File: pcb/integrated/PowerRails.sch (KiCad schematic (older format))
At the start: 28 parts, among them U9001 EC6AW, U9002 RAC10, U9003 TPS82140, U9004 TPS82140, U9005 TPS735, U9006 TPS735

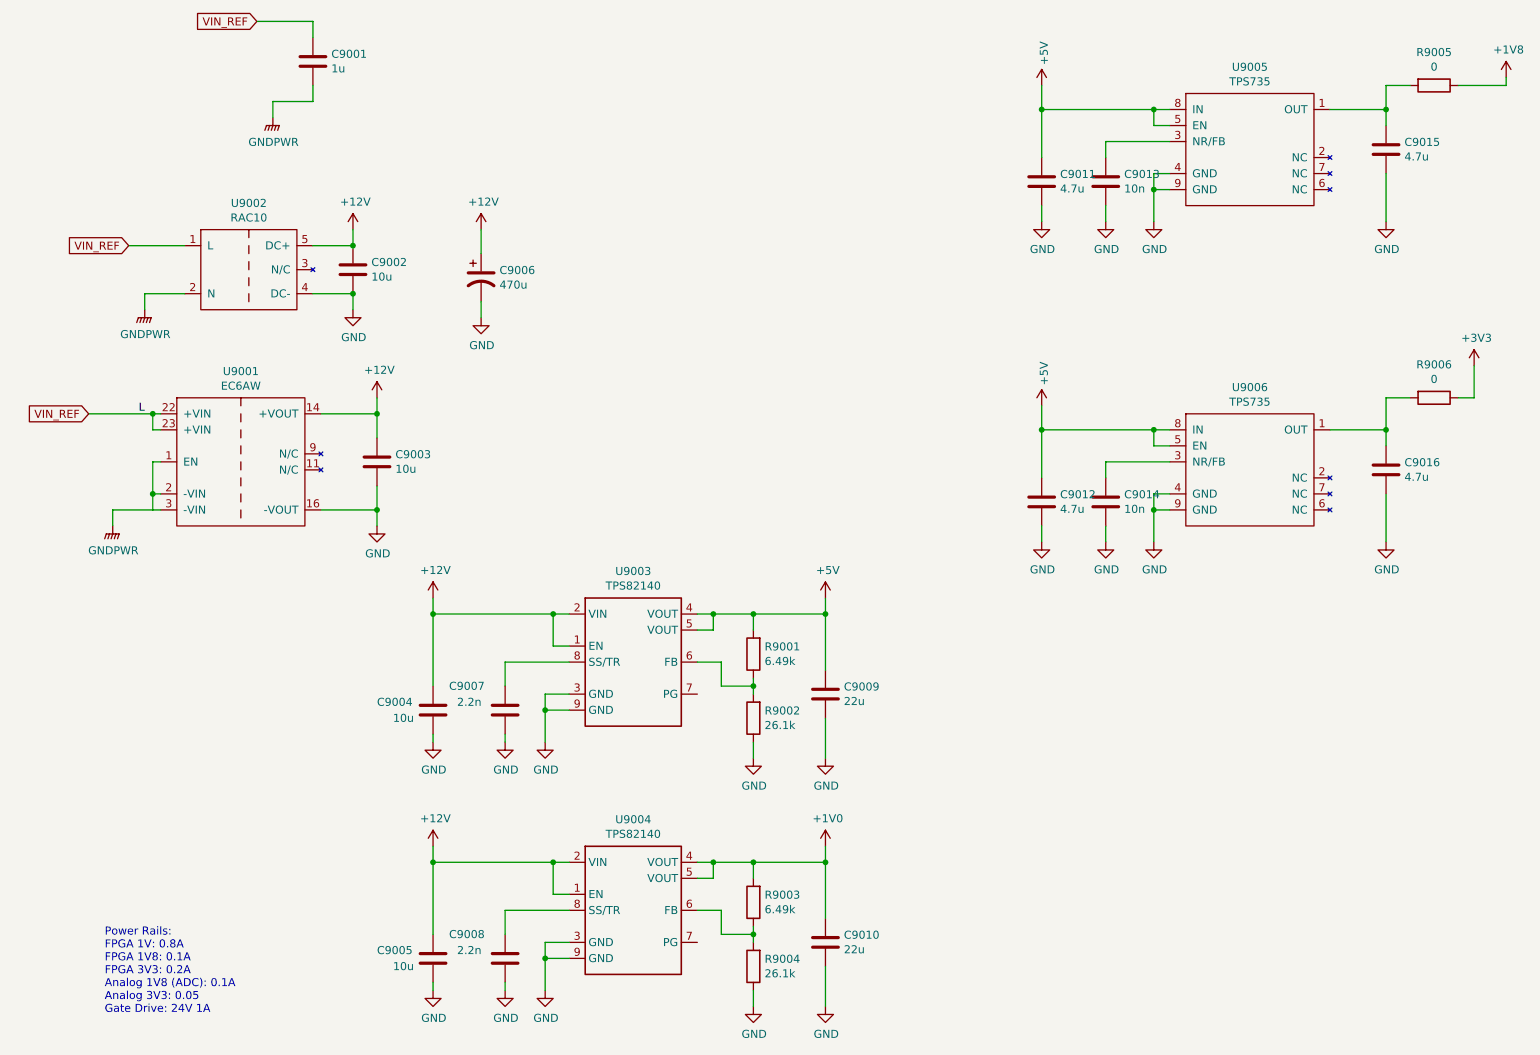
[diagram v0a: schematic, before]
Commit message: schematic fixes and component placement
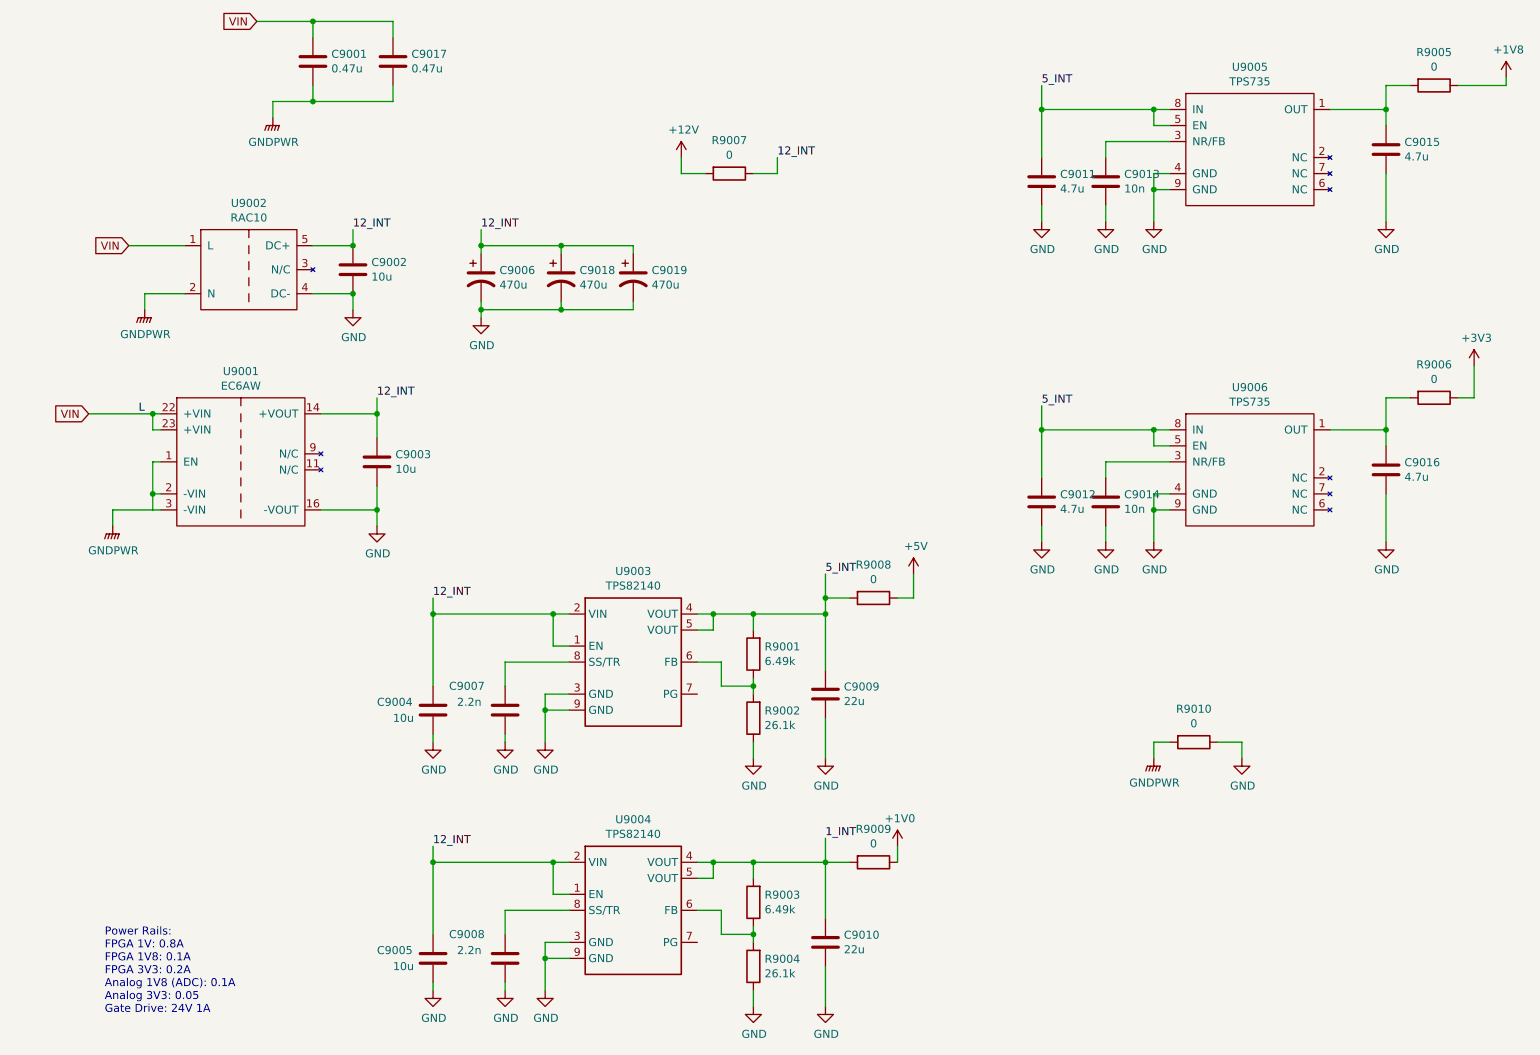
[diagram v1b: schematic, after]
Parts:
- added C9017: 0.47u, Capacitor_SMD:C_1812_4532Metric, symbol Device:C
- added C9018, C9019: 470u, Capacitor_THT:CP_Radial_D10.0mm_P5.00mm, symbol Device:CP1
- added R9007, R9008, R9009, R9010: 0, Resistor_SMD:R_0805_2012Metric, symbol Device:R
- C9001: value 1u -> 0.47u; footprint Capacitor_SMD:C_0805_2012Metric -> Capacitor_SMD:C_1812_4532Metric
- C9002, C9003, C9004, C9005: footprint Capacitor_SMD:C_0805_2012Metric -> Capacitor_SMD:C_1206_3216Metric
- C9007, C9008: footprint Capacitor_SMD:C_0805_2012Metric -> Capacitor_SMD:C_0402_1005Metric
- C9011, C9012, C9015, C9016: footprint Capacitor_SMD:C_0402_1005Metric -> Capacitor_SMD:C_0603_1608Metric
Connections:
- net +12V: now also R9007.2; no longer C9002.1, C9003.1, C9004.1, C9005.1, C9006.1, U9001.14 (+VOUT), U9002.5 (DC+), U9003.1 (EN), U9003.2 (VIN), U9004.1 (EN), U9004.2 (VIN)
- net +1V0: now also R9009.1; no longer C9010.1, R9003.2, U9004.4 (VOUT), U9004.5 (VOUT)
- net +5V: now also R9008.1; no longer C9009.1, C9011.2, C9012.2, R9001.2, U9003.4 (VOUT), U9003.5 (VOUT), U9005.5 (EN), U9005.8 (IN), U9006.5 (EN), U9006.8 (IN)
- net GND: now also C9018.2, C9019.2, R9010.1
- net GNDPWR: now also C9017.2, R9010.2
- net VIN_REF renamed VIN
- net VIN: now also C9017.1
- new net 12_INT: C9002.1, C9003.1, C9004.1, C9005.1, C9006.1, C9018.1, C9019.1, R9007.1, U9001.14 (+VOUT), U9002.5 (DC+), U9003.1 (EN), U9003.2 (VIN), U9004.1 (EN), U9004.2 (VIN)
- new net 1_INT: C9010.1, R9003.2, R9009.2, U9004.4 (VOUT), U9004.5 (VOUT)
- new net 5_INT: C9009.1, C9011.2, C9012.2, R9001.2, R9008.2, U9003.4 (VOUT), U9003.5 (VOUT), U9005.5 (EN), U9005.8 (IN), U9006.5 (EN), U9006.8 (IN)

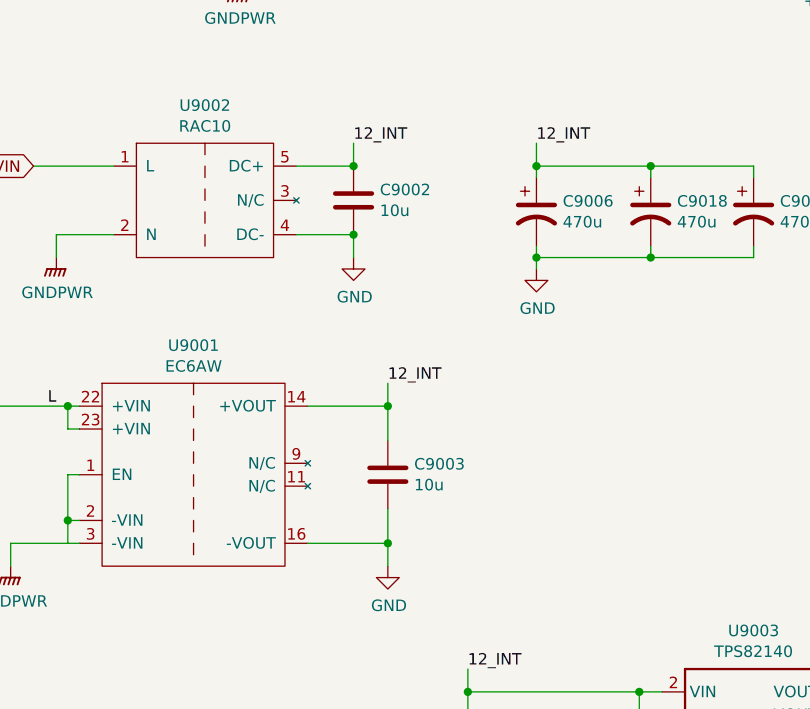
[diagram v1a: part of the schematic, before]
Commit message: routing, all componens placed on PCB
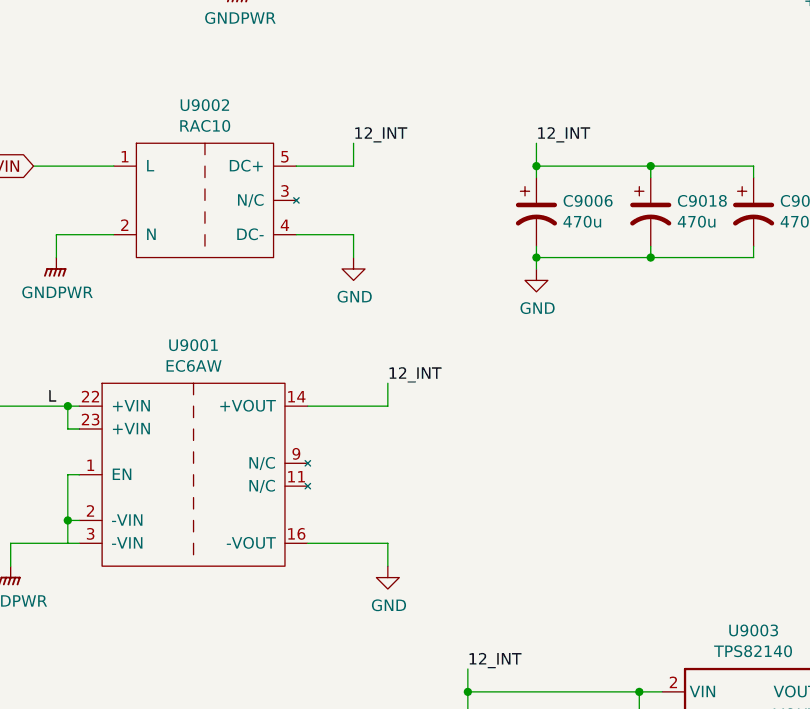
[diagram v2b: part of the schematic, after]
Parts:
- removed C9002, C9003: 10u, Capacitor_SMD:C_1206_3216Metric, symbol Device:C
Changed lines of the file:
@@
-	1    0    0    -1
-$EndComp
-$Comp
-L Device:C C9003
-U 1 1 5D6FA237
-P 3550 3750
-F 0 "C9003" H 3665 3796 50  0000 L CNN
-F 1 "10u" H 3665 3705 50  0000 L CNN
-F 2 "Capacitor_SMD:C_1206_3216Metric" H 3588 3600 50  0001 C CNN
-F 3 "~" H 3550 3750 50  0001 C CNN
-	1    3550 3750
-	1    0    0    -1
-$EndComp
-$Comp
-L Device:C C9002
-U 1 1 5D6FA2D9
-P 3400 2550
-F 0 "C9002" H 3515 2596 50  0000 L CNN
-F 1 "10u" H 3515 2505 50  0000 L CNN
-F 2 "Capacitor_SMD:C_1206_3216Metric" H 3438 2400 50  0001 C CNN
-F 3 "~" H 3400 2550 50  0001 C CNN
-	1    3400 2550
 	1    0    0    -1
 $EndComp
@@
 	3200 4050 3550 4050
 Wire Wire Line
-	3550 4050 3550 3900
-Wire Wire Line
 	3200 3450 3550 3450
 Wire Wire Line
-	3550 3450 3550 3600
-Wire Wire Line
 	3550 4050 3550 4150
-Connection ~ 3550 4050
 Wire Wire Line
 	3550 3450 3550 3350
-Connection ~ 3550 3450
 Wire Wire Line
 	3150 2700 3400 2700
@@
 Wire Wire Line
 	3400 2400 3400 2300
-Connection ~ 3400 2400
 Wire Wire Line
 	3400 2700 3400 2800
-Connection ~ 3400 2700
 $Comp
 L power:GND #PWR09003

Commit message: PCB routing finihsed, ready for design review
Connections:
- net VIN renamed VLINK
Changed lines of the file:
@@
 	1750 3450 2150 3450
 Text GLabel 2800 1000 0    50   Input ~ 0
-VIN
+VLINK
 $Comp
 L power:GNDPWR #PWR0103
@@
 	3650 1500 3650 1400
 Connection ~ 3150 1500
-Text GLabel 2000 2400 0    50   Input ~ 0
-VIN
-Text GLabel 1750 3450 0    50   Input ~ 0
-VIN
 $Comp
 L power:GND #PWR0177
@@
 Wire Wire Line
 	4700 2800 4200 2800
+Text GLabel 2000 2400 0    50   Input ~ 0
+VLINK
+Text GLabel 1750 3450 0    50   Input ~ 0
+VLINK
 $EndSCHEMATC

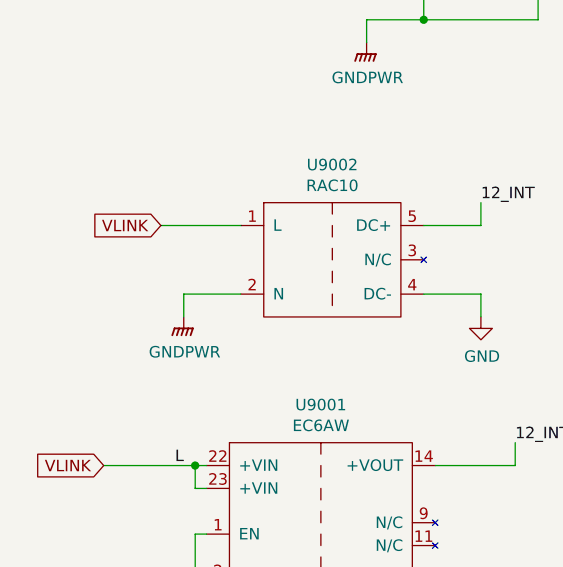
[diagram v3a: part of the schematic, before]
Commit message: finished design review and sent PCB to fab
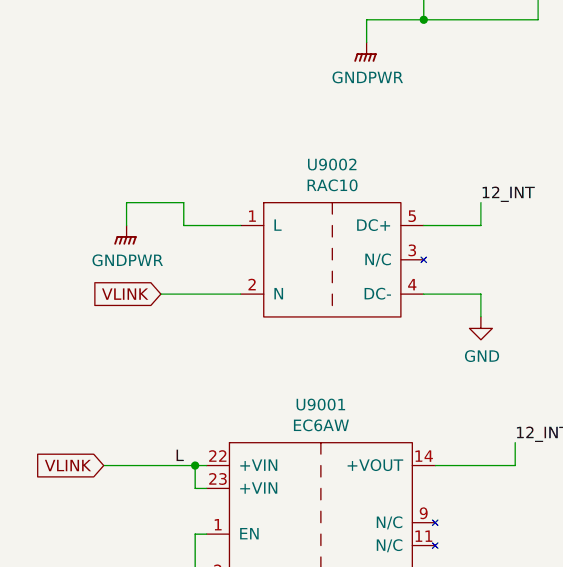
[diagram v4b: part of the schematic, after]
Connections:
- net GNDPWR: now also U9002.1 (L); no longer U9002.2 (N)
- net VLINK: now also U9002.2 (N); no longer U9002.1 (L)
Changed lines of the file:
@@
 L power:GNDPWR #PWR09001
 U 1 1 5D7359B7
-P 2100 2800
-F 0 "#PWR09001" H 2100 2600 50  0001 C CNN
-F 1 "GNDPWR" H 2104 2646 50  0000 C CNN
-F 2 "" H 2100 2750 50  0001 C CNN
-F 3 "" H 2100 2750 50  0001 C CNN
-	1    2100 2800
-	1    0    0    -1
-$EndComp
-Wire Wire Line
-	2100 2700 2100 2800
-Wire Wire Line
-	2000 2400 2350 2400
+P 1850 2400
+F 0 "#PWR09001" H 1850 2200 50  0001 C CNN
+F 1 "GNDPWR" H 1854 2246 50  0000 C CNN
+F 2 "" H 1850 2350 50  0001 C CNN
+F 3 "" H 1850 2350 50  0001 C CNN
+	1    1850 2400
+	1    0    0    -1
+$EndComp
+Wire Wire Line
+	1850 2300 1850 2400
+Wire Wire Line
+	2000 2700 2350 2700
 Wire Wire Line
 	3150 1000 3150 1100
@@
 	3150 1400 3150 1500
 Wire Wire Line
-	2100 2700 2350 2700
+	1850 2300 2100 2300
 $Comp
 L power:GNDPWR #PWR0102
@@
 Wire Wire Line
 	4700 2800 4200 2800
-Text GLabel 2000 2400 0    50   Input ~ 0
+Text GLabel 2000 2700 0    50   Input ~ 0
 VLINK
 Text GLabel 1750 3450 0    50   Input ~ 0
 VLINK
+Wire Wire Line
+	2350 2400 2100 2400
+Wire Wire Line
+	2100 2400 2100 2300
 $EndSCHEMATC
